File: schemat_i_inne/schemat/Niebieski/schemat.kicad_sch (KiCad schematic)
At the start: 34 parts, among them J1 Hole1, J2 Hole2, J3 Hole3, J4 Hole4, J5 RJ45, J6 Conn_01x01_Male, J7 Conn_01x01_Male, SW1 SW_DIP_x01, SW2 Left, SW3 Up, SW4 Down, SW5 Right, SW6 Jump, SW7 Punch, U1 ATmega32A-AU, U2 L7805, U3 WG12864B-STBL, U4 LF33_TO252, U5 SN74LS07, U6 SD, Y1 16Mhz

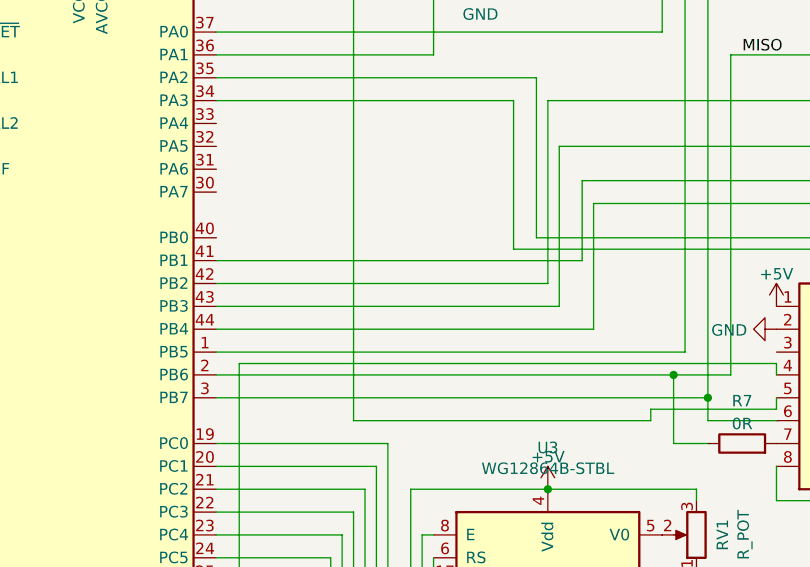
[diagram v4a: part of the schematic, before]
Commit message: Updated PCB ->key isn't anymore on PB4
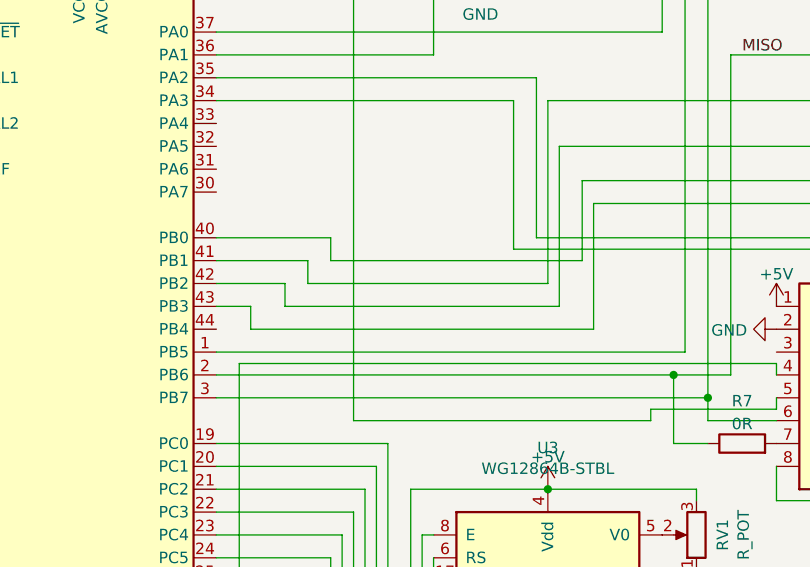
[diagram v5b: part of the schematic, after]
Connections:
- net at SW3.1: now also U1.42 (PB2); no longer U1.43 (PB3)
- net at SW4.1: now also U1.40 (PB0); no longer U1.41 (PB1)
- net at SW5.1: now also U1.41 (PB1); no longer U1.42 (PB2)
- net at SW2.1: now also U1.43 (PB3); no longer U1.44 (PB4)
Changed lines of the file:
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@@
+    (stroke (width 0) (type default) (color 0 0 0 0))
+  )
+  (wire (pts (xy 113.03 105.41) (xy 74.93 105.41))
     (stroke (width 0) (type default) (color 0 0 0 0))
   )
@@
     (stroke (width 0) (type default) (color 0 0 0 0))
   )
+  (wire (pts (xy 78.74 100.33) (xy 71.12 100.33))
+    (stroke (width 0) (type default) (color 0 0 0 0))
+  )
   (wire (pts (xy 209.55 95.25) (xy 209.55 152.4))
     (stroke (width 0) (type default) (color 0 0 0 0))
   )
+  (wire (pts (xy 78.74 102.87) (xy 78.74 100.33))
+    (stroke (width 0) (type default) (color 0 0 0 0))
+  )
   (wire (pts (xy 78.74 151.13) (xy 71.12 151.13))
     (stroke (width 0) (type default) (color 0 0 0 0))
@@
     (stroke (width 0) (type default) (color 0 0 0 0))
   )
-  (wire (pts (xy 111.76 97.79) (xy 71.12 97.79))
-    (stroke (width 0) (type default) (color 0 0 0 0))
-  )
   (wire (pts (xy 78.74 168.91) (xy 78.74 151.13))
     (stroke (width 0) (type default) (color 0 0 0 0))
@@
     (stroke (width 0) (type default) (color 0 0 0 0))
   )
-  (wire (pts (xy 113.03 105.41) (xy 71.12 105.41))
-    (stroke (width 0) (type default) (color 0 0 0 0))
-  )
   (wire (pts (xy 91.44 135.89) (xy 91.44 154.94))
     (stroke (width 0) (type default) (color 0 0 0 0))
@@
     (stroke (width 0) (type default) (color 0 0 0 0))
   )
+  (wire (pts (xy 107.95 100.33) (xy 81.28 100.33))
+    (stroke (width 0) (type default) (color 0 0 0 0))
+  )
   (wire (pts (xy 196.85 157.48) (xy 219.71 157.48))
     (stroke (width 0) (type default) (color 0 0 0 0))
   )
+  (wire (pts (xy 81.28 100.33) (xy 81.28 97.79))
+    (stroke (width 0) (type default) (color 0 0 0 0))
+  )
   (wire (pts (xy 124.46 124.46) (xy 124.46 123.19))
     (stroke (width 0) (type default) (color 0 0 0 0))
@@
     (stroke (width 0) (type default) (color 0 0 0 0))
   )
+  (wire (pts (xy 74.93 105.41) (xy 74.93 102.87))
+    (stroke (width 0) (type default) (color 0 0 0 0))
+  )
   (wire (pts (xy 80.01 153.67) (xy 71.12 153.67))
     (stroke (width 0) (type default) (color 0 0 0 0))
@@
     (stroke (width 0) (type default) (color 0 0 0 0))
   )
-  (wire (pts (xy 107.95 100.33) (xy 71.12 100.33))
-    (stroke (width 0) (type default) (color 0 0 0 0))
-  )
   (wire (pts (xy 121.92 156.21) (xy 121.92 170.18))
     (stroke (width 0) (type default) (color 0 0 0 0))
@@
     (stroke (width 0) (type default) (color 0 0 0 0))
   )
+  (wire (pts (xy 74.93 102.87) (xy 71.12 102.87))
+    (stroke (width 0) (type default) (color 0 0 0 0))
+  )
+  (wire (pts (xy 109.22 102.87) (xy 78.74 102.87))
+    (stroke (width 0) (type default) (color 0 0 0 0))
+  )
+  (wire (pts (xy 83.82 95.25) (xy 71.12 95.25))
+    (stroke (width 0) (type default) (color 0 0 0 0))
+  )
   (wire (pts (xy 45.72 182.88) (xy 49.53 182.88))
     (stroke (width 0) (type default) (color 0 0 0 0))
@@
     (stroke (width 0) (type default) (color 0 0 0 0))
   )
-  (wire (pts (xy 109.22 102.87) (xy 71.12 102.87))
+  (wire (pts (xy 81.28 97.79) (xy 71.12 97.79))
     (stroke (width 0) (type default) (color 0 0 0 0))
   )
@@
     (stroke (width 0) (type default) (color 0 0 0 0))
   )
+  (wire (pts (xy 111.76 97.79) (xy 83.82 97.79))
+    (stroke (width 0) (type default) (color 0 0 0 0))
+  )
   (wire (pts (xy 147.32 165.1) (xy 149.86 165.1))
     (stroke (width 0) (type default) (color 0 0 0 0))
@@
   )
   (wire (pts (xy 73.66 109.22) (xy 133.35 109.22))
+    (stroke (width 0) (type default) (color 0 0 0 0))
+  )
+  (wire (pts (xy 83.82 97.79) (xy 83.82 95.25))
     (stroke (width 0) (type default) (color 0 0 0 0))
   )
@@
       (effects (font (size 1.27 1.27)) hide)
     )
+    (pin "1")
+    (pin "2")
+    (pin "3")
+    (pin "4")
     (pin "5")
     (pin "6")
+    (pin "8")
+    (pin "9")
+    (pin "10")
+    (pin "11")
+    (pin "12")
+    (pin "13")
+    (pin "14")
+    (pin "7")
   )
   (symbol (lib_id "Device:R") (at 187.96 63.5 0) (unit 1)
@@
       (effects (font (size 1.27 1.27)) hide)
     )
+    (pin "1")
+    (pin "2")
+    (pin "3")
+    (pin "4")
+    (pin "5")
+    (pin "6")
+    (pin "8")
+    (pin "9")
+    (pin "10")
+    (pin "11")
+    (pin "12")
+    (pin "13")
     (pin "14")
     (pin "7")
@@
       (effects (font (size 1.27 1.27)) hide)
     )
+    (pin "1")
+    (pin "2")
+    (pin "3")
+    (pin "4")
+    (pin "5")
+    (pin "6")
     (pin "8")
     (pin "9")
+    (pin "10")
+    (pin "11")
+    (pin "12")
+    (pin "13")
+    (pin "14")
+    (pin "7")
   )
   (symbol (lib_id "power:GND") (at 157.48 175.26 0) (unit 1)
@@
     (pin "1")
     (pin "2")
+    (pin "3")
+    (pin "4")
+    (pin "5")
+    (pin "6")
+    (pin "8")
+    (pin "9")
+    (pin "10")
+    (pin "11")
+    (pin "12")
+    (pin "13")
+    (pin "14")
+    (pin "7")
   )
   (symbol (lib_id "Device:R") (at 137.16 49.53 90) (unit 1)
@@
       (effects (font (size 1.27 1.27)) hide)
     )
+    (pin "1")
+    (pin "2")
     (pin "3")
     (pin "4")
+    (pin "5")
+    (pin "6")
+    (pin "8")
+    (pin "9")
+    (pin "10")
+    (pin "11")
+    (pin "12")
+    (pin "13")
+    (pin "14")
+    (pin "7")
   )
   (symbol (lib_id "Device:R") (at 146.05 71.12 0) (unit 1)

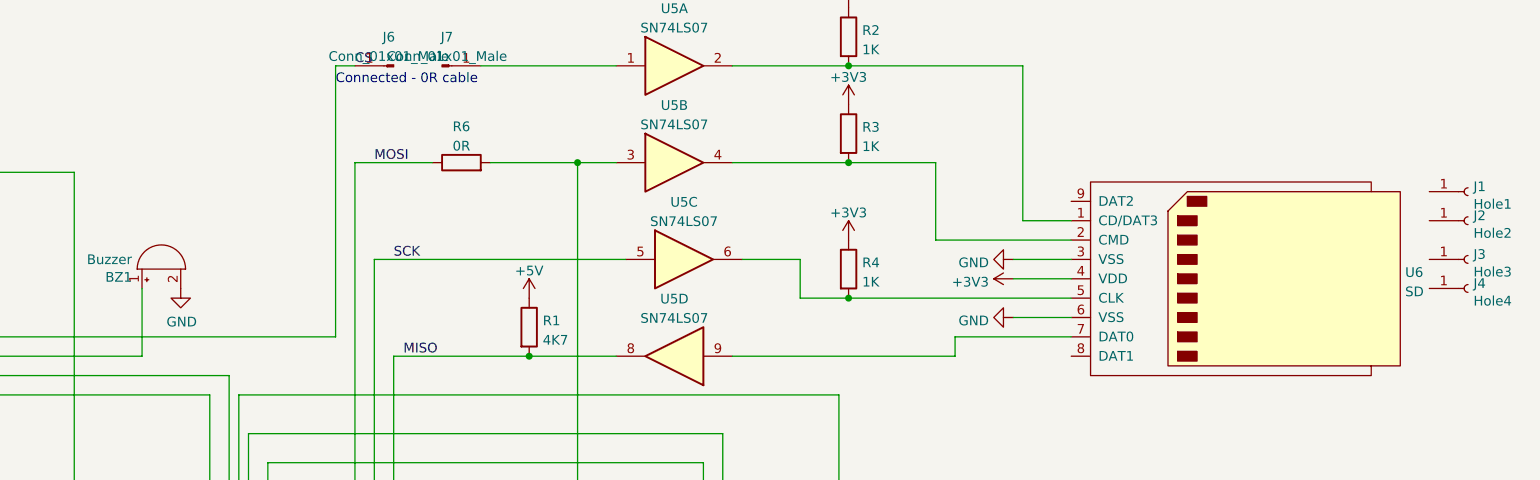
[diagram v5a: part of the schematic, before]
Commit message: Working CMake build and upload
use following comands
./configure.sh
./build.sh
./upload.sh
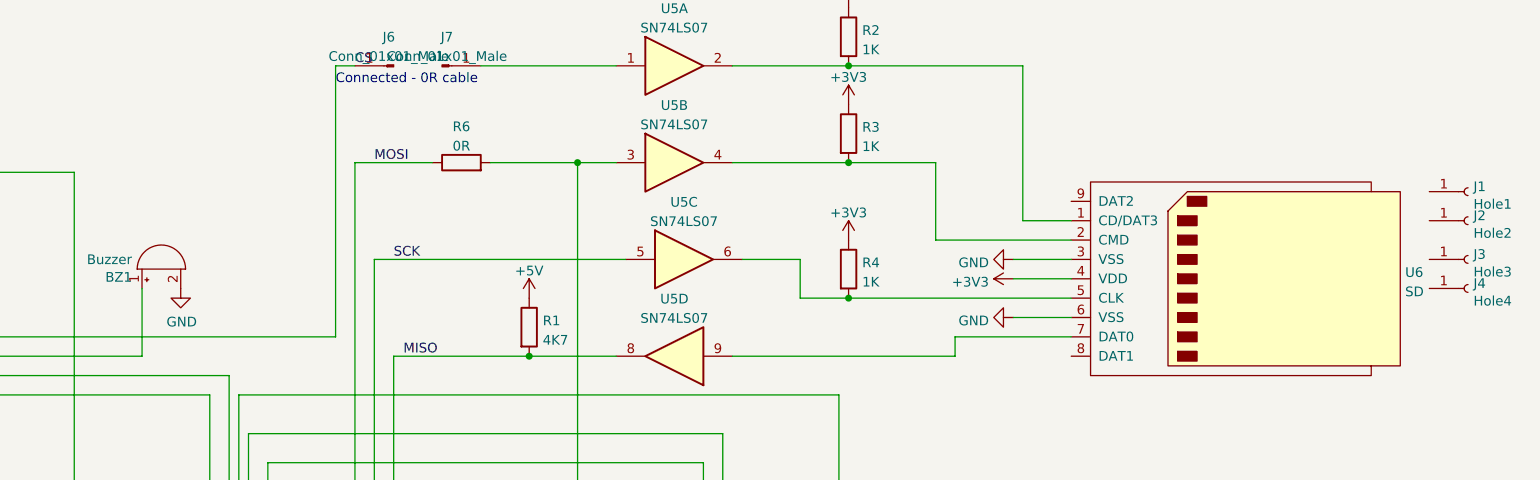
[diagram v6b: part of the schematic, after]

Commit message: new version of schema and board
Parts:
- removed J5: RJ45, Connector_RJ:RJ45_Amphenol_54602-x08_Horizontal, symbol Connector:RJ45
- removed J6, J7: Conn_01x01_Male, Connector_PinHeader_2.54mm:PinHeader_1x01_P2.54mm_Vertical, symbol Connector:Conn_01x01_Male
- removed R6: 0R, Resistor_THT:R_Axial_DIN0207_L6.3mm_D2.5mm_P10.16mm_Horizontal, symbol Device:R
- removed R7: 0R, Resistor_THT:R_Axial_DIN0204_L3.6mm_D1.6mm_P2.54mm_Vertical, symbol Device:R
- added C5: 100N, Capacitor_SMD:C_0805_2012Metric, symbol Device:C
- added D1: D, Diode_SMD:D_0201_0603Metric, symbol Device:D
- added J5: programming port, Connector_PinSocket_2.54mm:PinSocket_1x06_P2.54mm_Vertical, symbol Connector:Conn_01x06_Socket
- added J6: USB_B_Micro, Connector_USB:USB_Micro-AB_Molex_47590-0001, symbol Connector:USB_B_Micro
- added L1: 10uH, Inductor_SMD:L_6.3x6.3_H3, symbol Device:L
- added U7, U8: ~, joystick:joystickTHT, symbol joystick:joystickTHT
- BT1: footprint Connector_PinHeader_2.54mm:PinHeader_1x02_P2.54mm_Vertical -> Connector_PinSocket_2.54mm:PinSocket_1x02_P2.54mm_Vertical
- C1, C2, C3: footprint Connector_PinHeader_2.54mm:PinHeader_1x02_P2.54mm_Vertical -> Capacitor_SMD:C_0805_2012Metric
- C4: footprint Connector_PinHeader_2.54mm:PinHeader_1x02_P2.54mm_Vertical -> Capacitor_SMD:CP_Elec_6.3x5.4_Nichicon
- SW1: footprint Connector_PinHeader_2.54mm:PinHeader_1x03_P2.54mm_Vertical -> Button_Switch_SMD:SW_DIP_SPSTx01_Slide_Copal_CVS-01xB_W5.9mm_P1mm
- SW2: value Left -> Home; footprint Button_Switch_THT:SW_PUSH-12mm -> Button_Switch_SMD:SW_Push_1P1T_NO_6x6mm_H9.5mm
- SW3: value Up -> triggerR; footprint Button_Switch_THT:SW_PUSH-12mm -> Button_Switch_THT:SW_Tactile_SPST_Angled_PTS645Vx31-2LFS
- SW4: value Down -> Select; footprint Button_Switch_THT:SW_PUSH-12mm -> Button_Switch_SMD:SW_Push_1P1T_NO_6x6mm_H9.5mm
- SW5: value Right -> triggerL; footprint Button_Switch_THT:SW_PUSH-12mm -> Button_Switch_THT:SW_Tactile_SPST_Angled_PTS645Vx31-2LFS
- SW6: value Jump -> BumperL; footprint Button_Switch_THT:SW_PUSH-12mm -> Button_Switch_THT:SW_Tactile_SPST_Angled_PTS645Vx31-2LFS
- SW7: value Punch -> BumperR; footprint Button_Switch_THT:SW_PUSH-12mm -> Button_Switch_THT:SW_Tactile_SPST_Angled_PTS645Vx31-2LFS
- U1: value ATmega32A-AU -> ATmega1284P
- U2: footprint Package_TO_SOT_THT:TO-220-3_Vertical -> Package_TO_SOT_SMD:TO-252-2
- U5: footprint Package_DIP:DIP-14_W7.62mm_LongPads -> Package_SO:SO-14_3.9x8.65mm_P1.27mm
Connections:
- net SCK is gone; now on net MISO: U1.3 (PB7), U5.5
- net +5V: now also SW2.1, SW3.1, SW4.1, SW5.2, SW6.2, SW7.1, J5.5 (Pin_5), J6.1 (VBUS), L1.1, U7.1 (P11), U7.6 (P23), U8.1 (P11), U8.6 (P23); no longer U1.27 (AVCC)
- net CS: now also U1.44 (PB4), U5.1; no longer U1.37 (PA0)
- net GND: now also C5.2, J5.6 (Pin_6), J6.5 (GND), J6.6 (Shield), U7.3 (P13), U7.4 (P21), U8.3 (P13), U8.4 (P21); no longer SW2.2, SW3.2, SW4.2, SW5.2, SW6.2, SW7.2
- net MISO: now also J5.2 (Pin_2), J5.3 (Pin_3)
- net MOSI: now also U5.3, J5.1 (Pin_1)
- net at U1.42 (PB2): now also SW4.2; no longer SW3.1
- net at U1.40 (PB0): no longer SW4.1
- net at SW5.1: now also U1.11 (PD2); no longer U1.41 (PB1)
- net at U1.43 (PB3): now also BZ1.1 (-); no longer SW2.1
- net at SW6.1: now also U1.33 (PA4); no longer U1.35 (PA2)
- net at U1.34 (PA3): now also U8.2 (P12); no longer SW7.1
- net at U1.10 (PD1): now also SW7.2
- net at U1.29 (AREF): now also C5.1
- net at U1.32 (PA5): now also SW3.2
- net at U1.36 (PA1): now also U7.2 (P12); no longer BZ1.1 (-)
- net at U1.4 (~{RESET}): now also J5.4 (Pin_4)
- net at U1.9 (PD0): now also SW2.2
- net at C1.1, U2.1 (IN): now also D1.1 (K); no longer SW1.1
- new net: L1.2, U1.27 (AVCC)
- new net: U1.35 (PA2), U8.5 (P22)
- new net: U1.37 (PA0), U7.5 (P22)
- new net: D1.2 (A), SW1.1
- no-connect marks 0 -> 3
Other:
- note removed: "Connected - 0R cable"
- moved on the sheet: BZ1, C1, C2, R1, R2, R3, R4, RV1, U1, U2, U3, U5A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
